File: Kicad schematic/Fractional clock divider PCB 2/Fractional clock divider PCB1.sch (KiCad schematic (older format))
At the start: 73 parts, among them J1 Conn_01x06_Female, J2 Conn_01x06_Male, J3 Conn_01x15_Male, J4 Conn_01x15_Female, J5 Conn_01x09_Female, J6 Conn_01x09_Male, Q1 2N3904, Q2 2N3904, Q3 2N3904, Q4 2N3904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

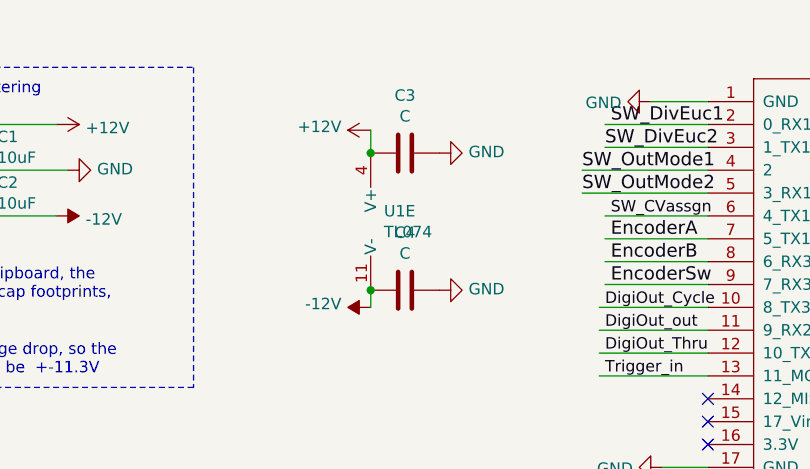
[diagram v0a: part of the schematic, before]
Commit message: Code update to reflect PCB design
Updating code to reflect
-changes in pins
-new CV assignment method
-new mode slect configuration

Seems to work, but having assembled the first version of the PCB there's quite a few errors to fix before we take development any further...
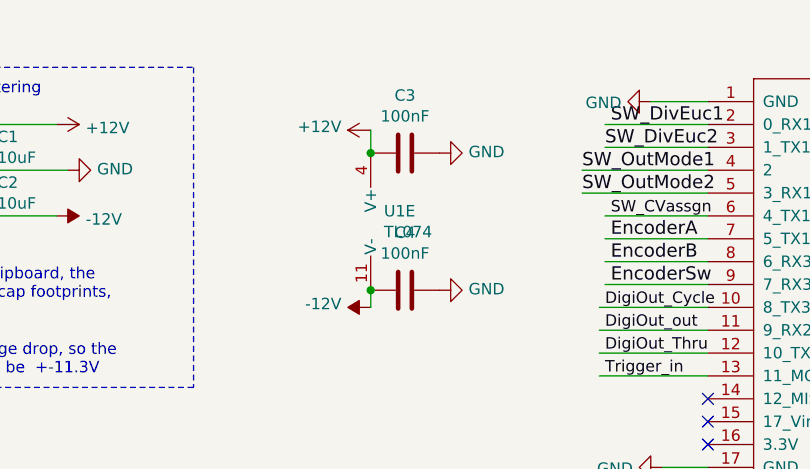
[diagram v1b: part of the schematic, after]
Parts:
- C3, C4: value C -> 100nF
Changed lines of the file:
@@
 P 5575 1825
 F 0 "C4" V 5827 1825 50  0000 C CNN
-F 1 "C" V 5736 1825 50  0000 C CNN
+F 1 "100nF" V 5736 1825 50  0000 C CNN
 F 2 "Capacitor_THT:C_Rect_L11.5mm_W4.0mm_P10.00mm_MKT" H 5613 1675 50  0001 C CNN
 F 3 "~" H 5575 1825 50  0001 C CNN
@@
 P 5575 1225
 F 0 "C3" V 5323 1225 50  0000 C CNN
-F 1 "C" V 5414 1225 50  0000 C CNN
+F 1 "100nF" V 5414 1225 50  0000 C CNN
 F 2 "Capacitor_THT:C_Rect_L11.5mm_W4.0mm_P10.00mm_MKT" H 5613 1075 50  0001 C CNN
 F 3 "~" H 5575 1225 50  0001 C CNN
